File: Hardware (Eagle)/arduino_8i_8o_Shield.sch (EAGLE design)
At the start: 15 parts, among them IC1 ULN2803

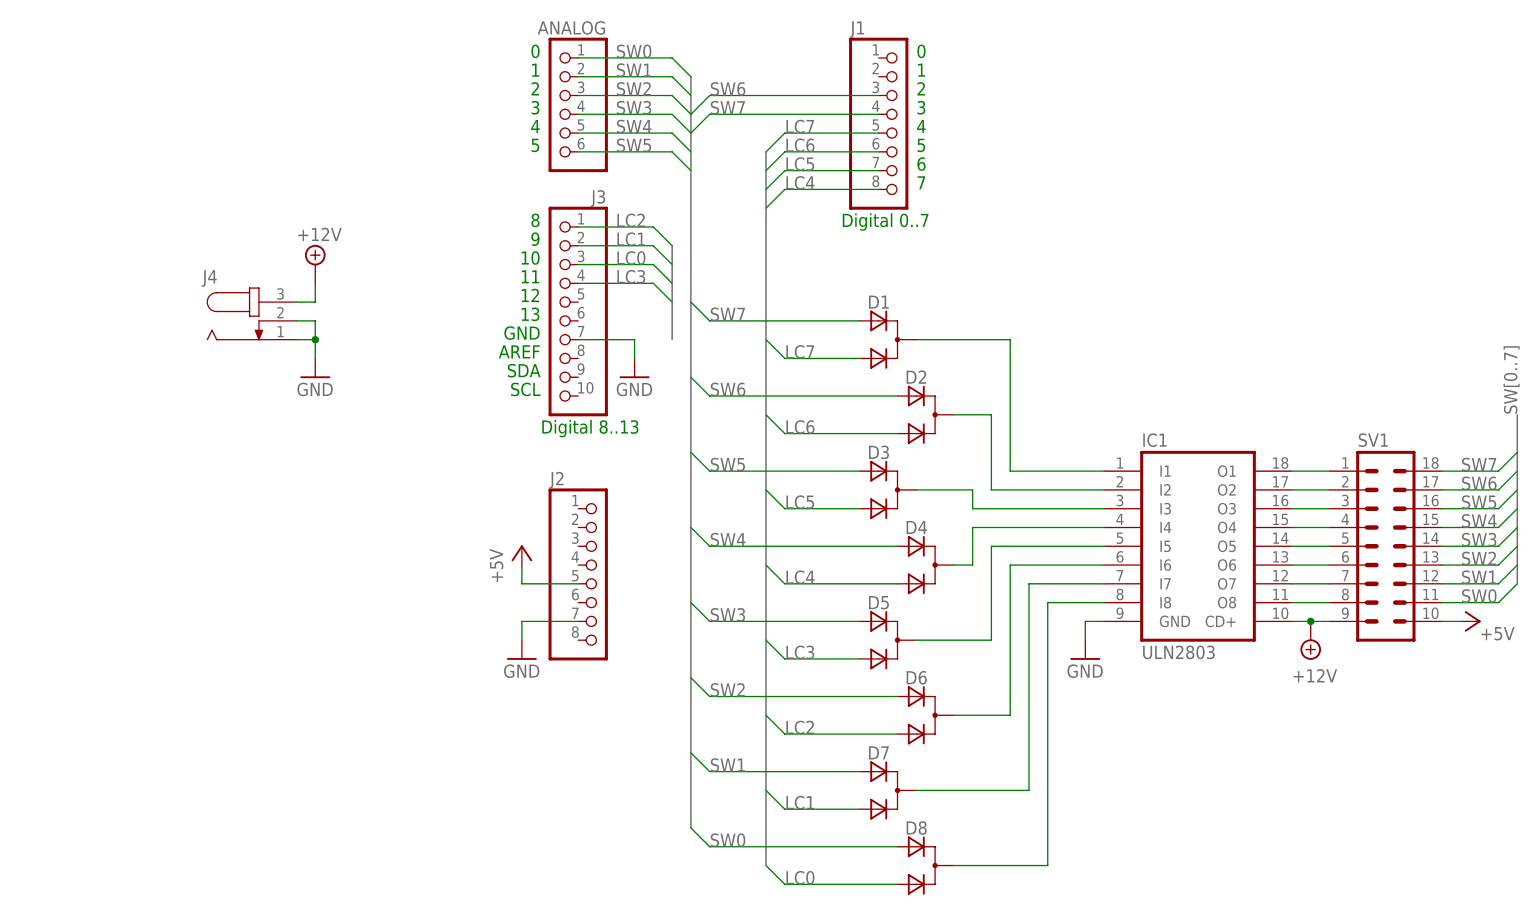
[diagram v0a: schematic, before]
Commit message: Added 8 x 18k pull-down resistors on switches inputs
The absence of these resistors induced a cross talk between LED output
and switches reading inputs
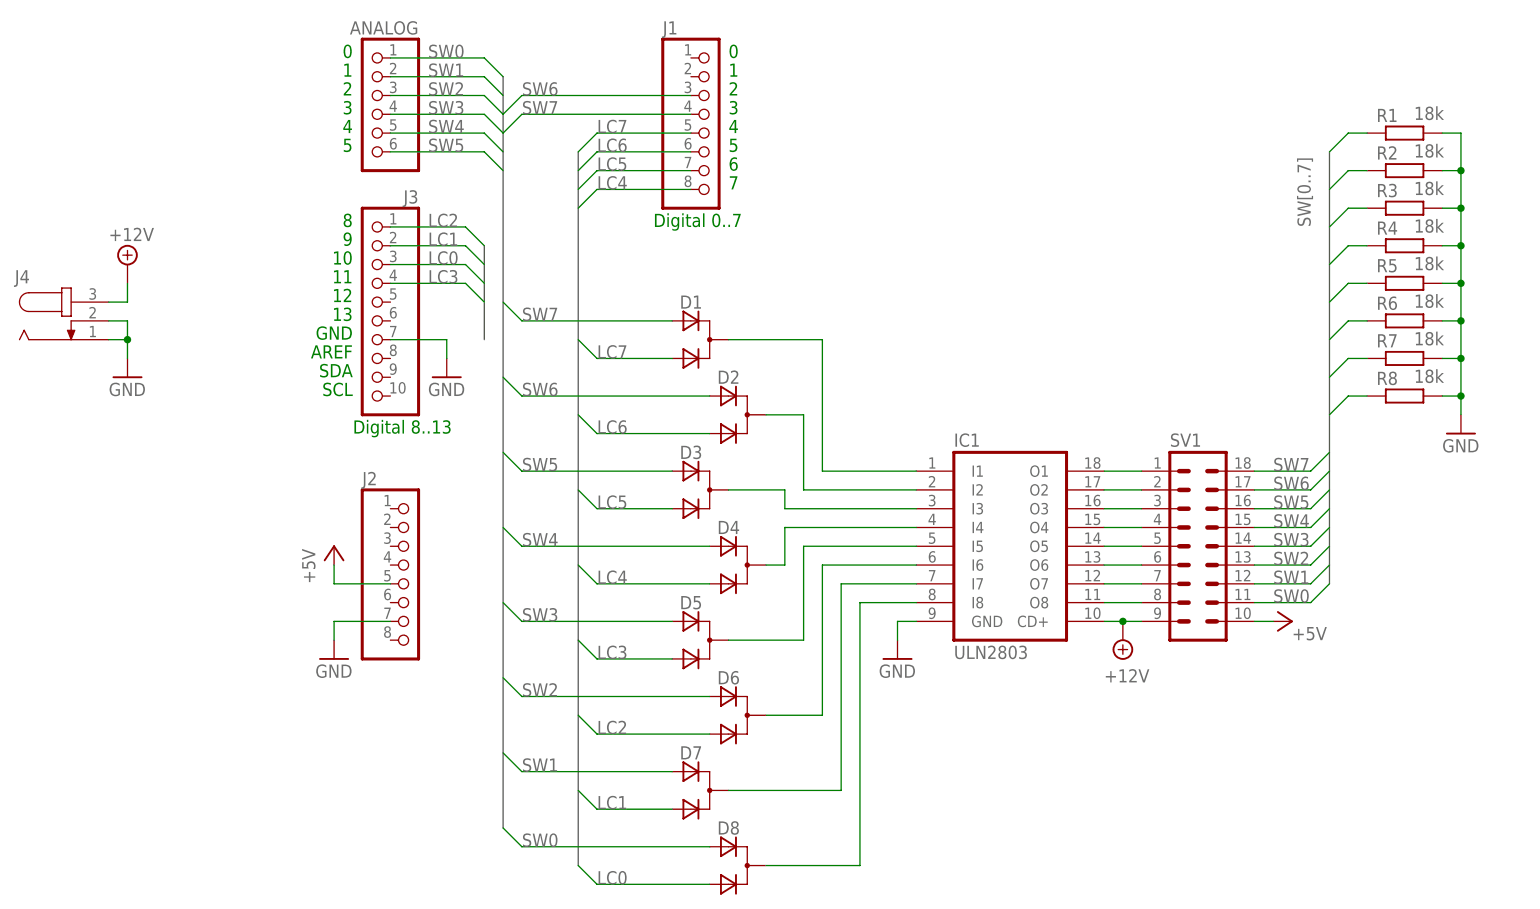
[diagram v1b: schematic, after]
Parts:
- added R1, R2, R3, R4, R5, R6, R7, R8: 18k, rcl:R-EU_M1206
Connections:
- net GND: now also R1.2, R2.2, R3.2, R4.2, R5.2, R6.2, R7.2, R8.2
- net SW0: now also R1.1
- net SW1: now also R2.1
- net SW2: now also R3.1
- net SW3: now also R4.1
- net SW4: now also R5.1
- net SW5: now also R6.1
- net SW6: now also R7.1
- net SW7: now also R8.1
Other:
- moved on the sheet: ANALOG, D1, D2, D3, D4, D5, D6, D7, D8, IC1, J1, J2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
